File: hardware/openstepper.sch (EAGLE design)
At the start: 20 parts, among them IC1 DARLINGTON_ARRAY, J1 CON_HEADER_1X06-PTH, J3 CON_HEADER_1X04, J4 CON_HEADER_1X02-PTH, U1 IC_PCA9629A

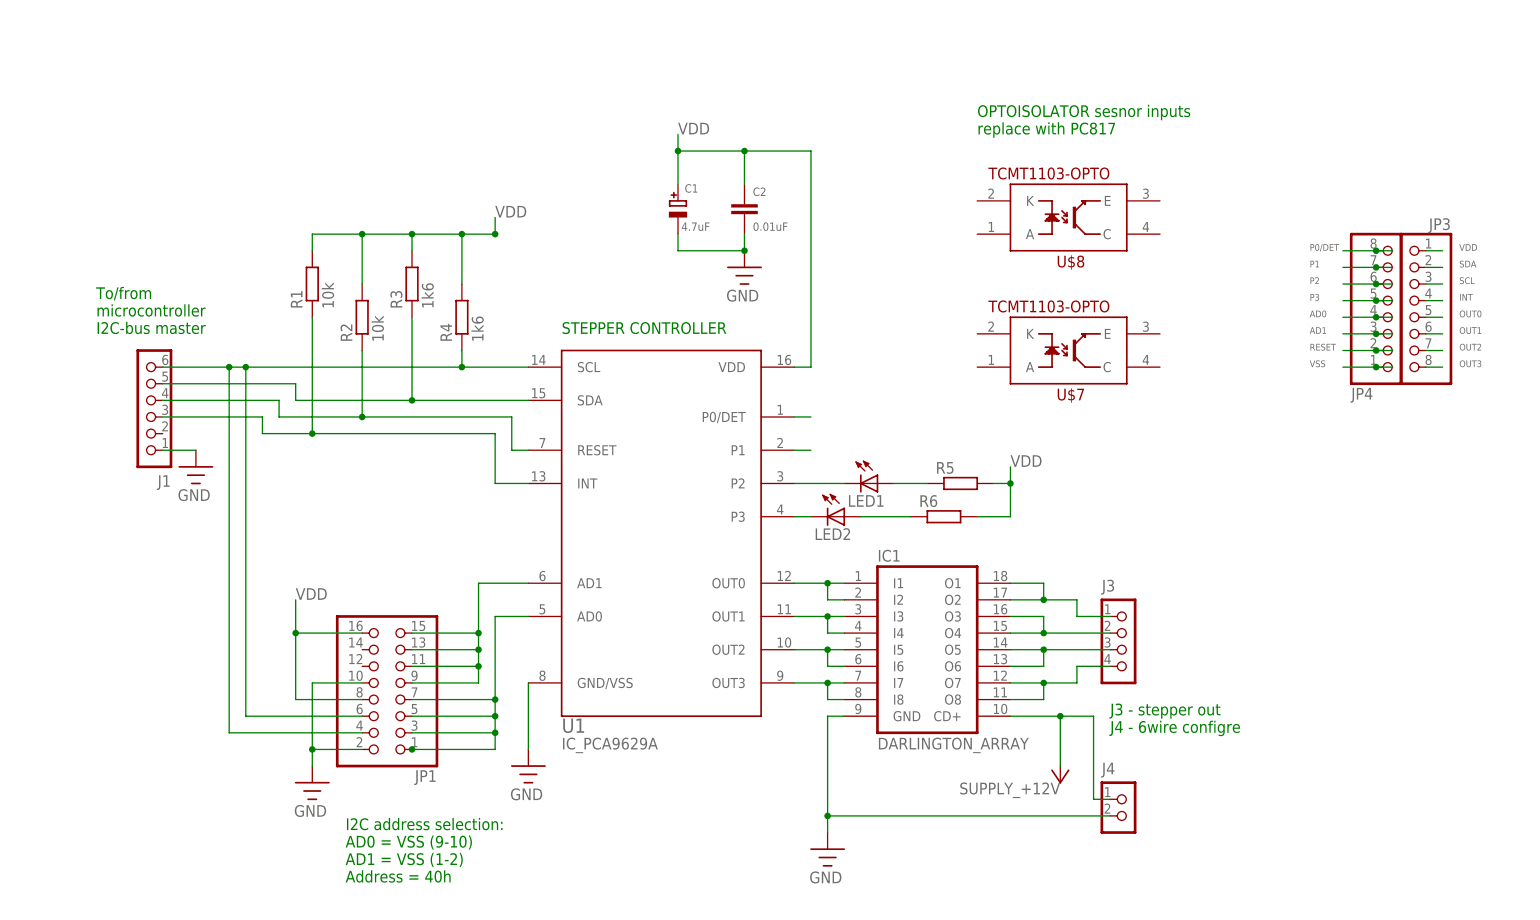
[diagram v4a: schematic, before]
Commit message: added 5v regulator to schema
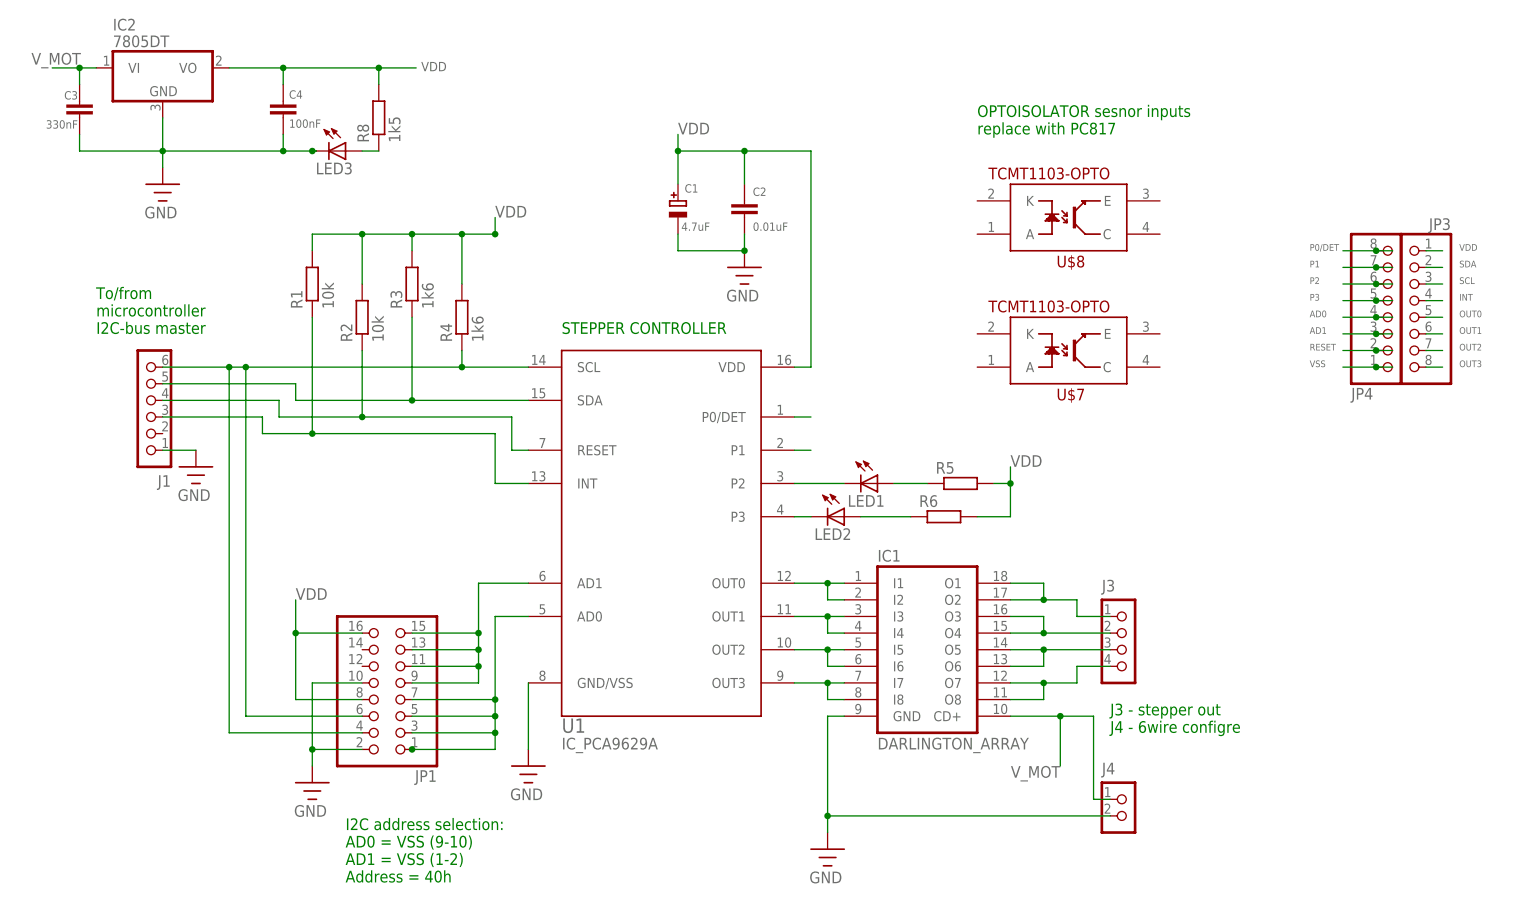
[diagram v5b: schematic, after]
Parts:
- added C3: 330nF, rcl:C-EU025-024X044
- added C4: 100nF, rcl:C-EU025-024X044
- added IC2: 7805DT, adafruit:7805DT
- added LED3: (no value), dp_devices:LED-0805
- added R8: 1k5, dp_devices:RESISTOR-1206
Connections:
- removed net +12V: IC1.CD+, J4.1
- new net N$1: LED3.A, R8.1
- new net V_MOT: C3.2, IC1.CD+, IC2.VI, J4.1
- net GND: now also C3.1, C4.1, IC2.GND, LED3.C
- net VDD: now also C4.2, IC2.VO, R8.2
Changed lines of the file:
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@@
 <part name="U$2" library="openstepper" deviceset="GND" device=""/>
 <part name="U$3" library="openstepper" deviceset="GND" device=""/>
-<part name="+12V1" library="dp_devices" deviceset="SUPPLY_+12V" device=""/>
 <part name="J3" library="dp_devices" deviceset="CON_HEADER_1X04" device=""/>
 <part name="J1" library="dp_devices" deviceset="CON_HEADER_1X06" device="-PTH"/>
@@
 <part name="JP3" library="adafruit" deviceset="PINHD-1X8" device="BIG"/>
 <part name="JP4" library="adafruit" deviceset="PINHD-1X8" device="BIG"/>
+<part name="C3" library="rcl" deviceset="C-EU" device="025-024X044" value="330nF"/>
+<part name="C4" library="rcl" deviceset="C-EU" device="025-024X044" value="100nF"/>
+<part name="R8" library="dp_devices" deviceset="RESISTOR" device="-1206" value="1k5"/>
+<part name="LED3" library="dp_devices" deviceset="LED" device="-0805"/>
+<part name="IC2" library="adafruit" deviceset="78*" device="DT" technology="05"/>
+<part name="U$5" library="openstepper" deviceset="GND" device=""/>
 </parts>
 <sheets>
@@
 <instance part="U$2" gate="G$1" x="66.04" y="17.78"/>
 <instance part="U$3" gate="G$1" x="111.76" y="5.08"/>
-<instance part="+12V1" gate="SUPPLY" x="147.32" y="17.78" rot="R180"/>
 <instance part="J3" gate="J" x="154.94" y="38.1"/>
 <instance part="J1" gate="J" x="10.16" y="71.12" rot="R180"/>
@@
 <instance part="JP3" gate="G$1" x="200.66" y="88.9" rot="MR0"/>
 <instance part="JP4" gate="G$1" x="198.12" y="86.36" rot="MR180"/>
+<instance part="C3" gate="G$1" x="-2.54" y="116.84" smashed="yes" rot="R180">
+<attribute name="NAME" x="-2.794" y="120.904" size="1.27" layer="95" rot="R180"/>
+<attribute name="VALUE" x="-2.794" y="116.459" size="1.27" layer="96" rot="R180"/>
+</instance>
+<instance part="C4" gate="G$1" x="28.575" y="116.84" smashed="yes" rot="R180">
+<attribute name="NAME" x="29.464" y="119.761" size="1.27" layer="95"/>
+<attribute name="VALUE" x="29.464" y="115.316" size="1.27" layer="96"/>
+</instance>
+<instance part="R8" gate="G$1" x="43.18" y="116.84" rot="R90"/>
+<instance part="LED3" gate="LED" x="38.1" y="111.76" rot="R270"/>
+<instance part="IC2" gate="A1" x="10.16" y="124.46"/>
+<instance part="U$5" gate="G$1" x="10.16" y="106.68"/>
 </instances>
 <busses>
@@
 <wire x1="33.02" y1="30.48" x2="40.64" y2="30.48" width="0.1524" layer="91"/>
 </segment>
-</net>
-<net name="+12V" class="0">
-<segment>
-<pinref part="IC1" gate="IC" pin="CD+"/>
-<pinref part="+12V1" gate="SUPPLY" pin="+12V"/>
-<wire x1="139.7" y1="25.4" x2="147.32" y2="25.4" width="0.1524" layer="91"/>
-<wire x1="147.32" y1="25.4" x2="147.32" y2="17.78" width="0.1524" layer="91"/>
-<wire x1="147.32" y1="25.4" x2="152.4" y2="25.4" width="0.1524" layer="91"/>
-<wire x1="152.4" y1="25.4" x2="152.4" y2="12.7" width="0.1524" layer="91"/>
-<junction x="147.32" y="25.4"/>
-<pinref part="J4" gate="J" pin="1"/>
-<wire x1="152.4" y1="12.7" x2="154.94" y2="12.7" width="0.1524" layer="91"/>
+<segment>
+<wire x1="-2.54" y1="114.3" x2="-2.54" y2="111.76" width="0.1524" layer="91"/>
+<wire x1="-2.54" y1="111.76" x2="10.16" y2="111.76" width="0.1524" layer="91"/>
+<wire x1="10.16" y1="111.76" x2="28.575" y2="111.76" width="0.1524" layer="91"/>
+<wire x1="28.575" y1="111.76" x2="28.575" y2="114.3" width="0.1524" layer="91"/>
+<wire x1="33.655" y1="111.76" x2="33.02" y2="111.76" width="0.1524" layer="91"/>
+<wire x1="33.02" y1="111.76" x2="28.575" y2="111.76" width="0.1524" layer="91"/>
+<junction x="28.575" y="111.76"/>
+<pinref part="C4" gate="G$1" pin="1"/>
+<pinref part="C3" gate="G$1" pin="1"/>
+<pinref part="LED3" gate="LED" pin="C"/>
+<junction x="33.02" y="111.76"/>
+<pinref part="IC2" gate="A1" pin="GND"/>
+<wire x1="10.16" y1="116.84" x2="10.16" y2="111.76" width="0.1524" layer="91"/>
+<junction x="10.16" y="111.76"/>
+<pinref part="U$5" gate="G$1" pin="GND"/>
+<wire x1="10.16" y1="111.76" x2="10.16" y2="109.22" width="0.1524" layer="91"/>
 </segment>
 </net>
@@
 <pinref part="JP3" gate="G$1" pin="1"/>
 </segment>
+<segment>
+<wire x1="48.895" y1="124.46" x2="43.18" y2="124.46" width="0.1524" layer="91"/>
+<wire x1="43.18" y1="124.46" x2="28.575" y2="124.46" width="0.1524" layer="91"/>
+<wire x1="28.575" y1="121.92" x2="28.575" y2="124.46" width="0.1524" layer="91"/>
+<wire x1="28.575" y1="124.46" x2="20.32" y2="124.46" width="0.1524" layer="91"/>
+<junction x="28.575" y="124.46"/>
+<label x="49.657" y="123.952" size="1.4224" layer="95"/>
+<pinref part="C4" gate="G$1" pin="2"/>
+<pinref part="R8" gate="G$1" pin="2"/>
+<wire x1="43.18" y1="121.92" x2="43.18" y2="124.46" width="0.1524" layer="91"/>
+<junction x="43.18" y="124.46"/>
+<pinref part="IC2" gate="A1" pin="VO"/>
+</segment>
 </net>
 <net name="N$11" class="0">
@@
 </segment>
 </net>
+<net name="V_MOT" class="0">
+<segment>
+<pinref part="IC2" gate="A1" pin="VI"/>
+<wire x1="-6.731" y1="124.46" x2="-2.54" y2="124.46" width="0.1524" layer="91"/>
+<label x="-9.906" y="124.968" size="1.778" layer="95"/>
+<wire x1="-2.54" y1="124.46" x2="0" y2="124.46" width="0.1524" layer="91"/>
+<wire x1="-2.54" y1="121.92" x2="-2.54" y2="124.46" width="0.1524" layer="91"/>
+<junction x="-2.54" y="124.46"/>
+<pinref part="C3" gate="G$1" pin="2"/>
+</segment>
+<segment>
+<pinref part="IC1" gate="IC" pin="CD+"/>
+<wire x1="139.7" y1="25.4" x2="147.32" y2="25.4" width="0.1524" layer="91"/>
+<wire x1="147.32" y1="25.4" x2="147.32" y2="17.78" width="0.1524" layer="91"/>
+<wire x1="147.32" y1="25.4" x2="152.4" y2="25.4" width="0.1524" layer="91"/>
+<wire x1="152.4" y1="25.4" x2="152.4" y2="12.7" width="0.1524" layer="91"/>
+<junction x="147.32" y="25.4"/>
+<pinref part="J4" gate="J" pin="1"/>
+<wire x1="152.4" y1="12.7" x2="154.94" y2="12.7" width="0.1524" layer="91"/>
+<label x="147.32" y="17.78" size="1.778" layer="95" rot="R180"/>
+</segment>
+</net>
+<net name="N$1" class="0">
+<segment>
+<pinref part="LED3" gate="LED" pin="A"/>
+<pinref part="R8" gate="G$1" pin="1"/>
+<wire x1="40.64" y1="111.76" x2="43.18" y2="111.76" width="0.1524" layer="91"/>
+</segment>
+</net>
